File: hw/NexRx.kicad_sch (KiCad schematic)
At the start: 12 parts, among them J101 SMA

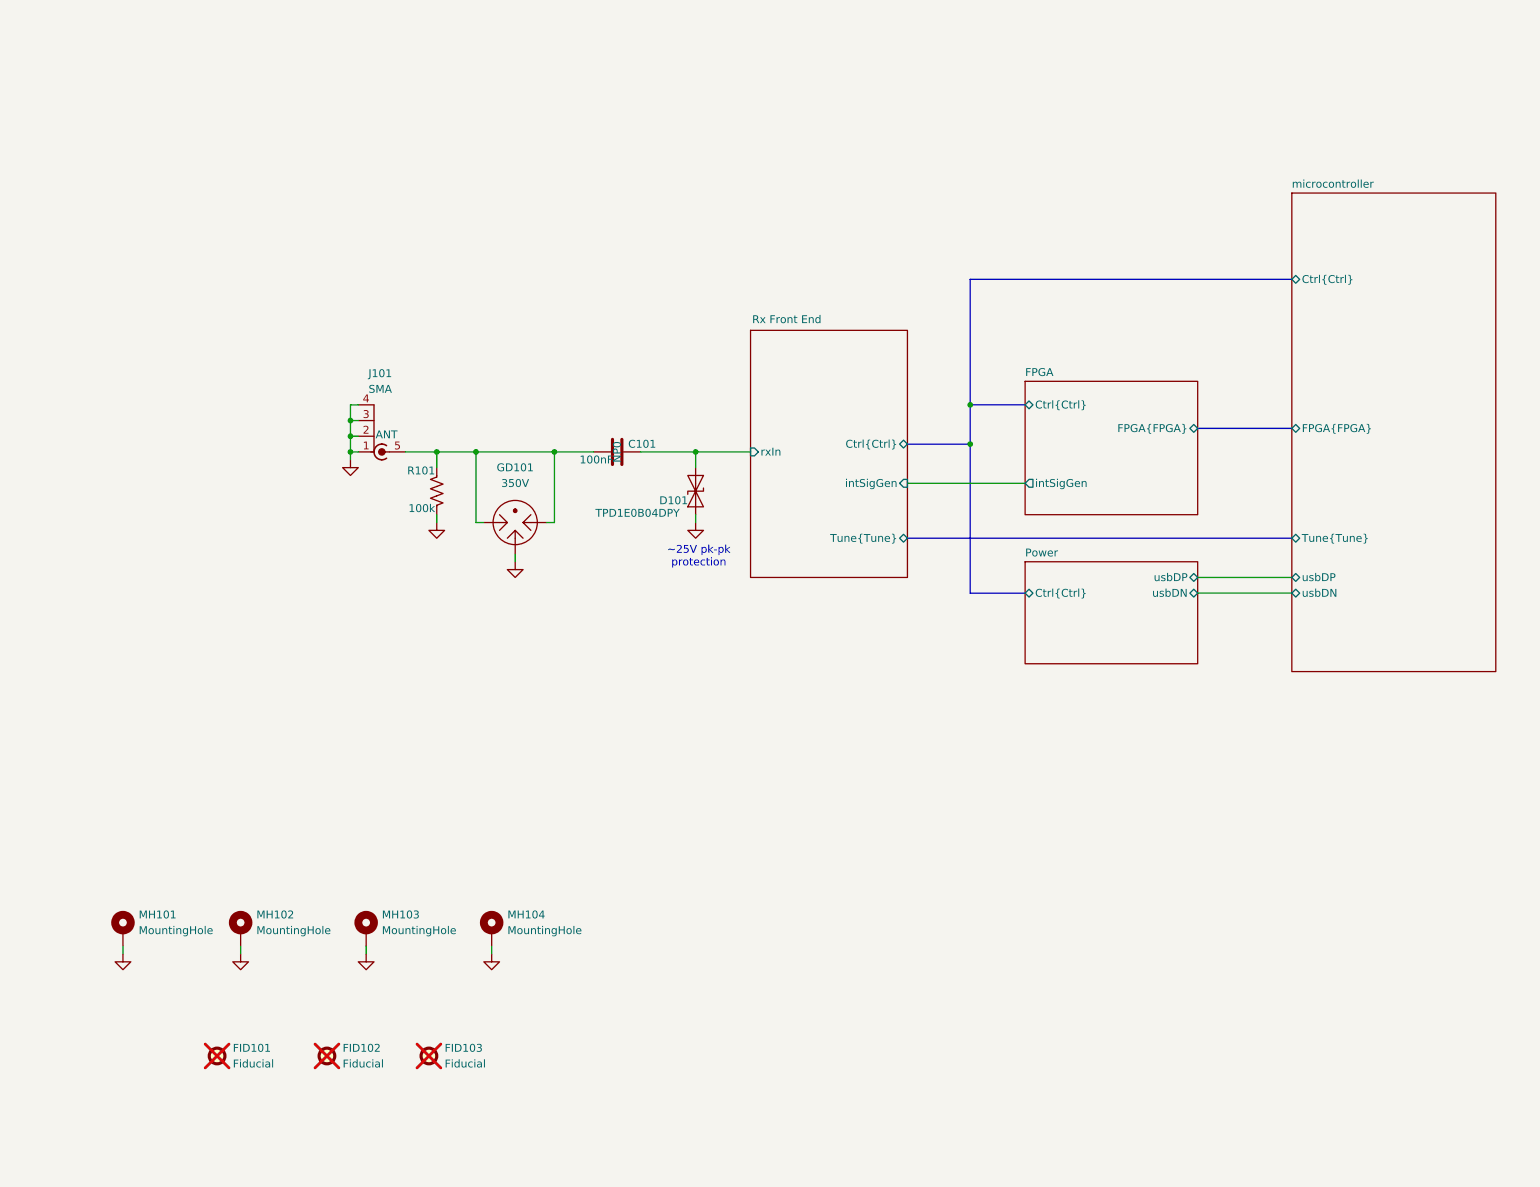
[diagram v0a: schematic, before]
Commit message: Switch from three QSDs to two Octature Sync Detectors (OSDs) and use one 4-channel TI ADC for each. Simplify. Refactor busses to use cleaner notation and modularity. Switch to a CPLD from FPGA. Eliminate STM32C011 GPIO expanders (maybe need them back later?). Power sequencing is now trivial and there is no 5VA so no boost to more than 5V then LDO back down to 5V. Merge some pages into one. Change to 74CBTLV3125 for OSD switches (four for each OSD). Elminate MAX9939 PGA since ADC has this feature. Filter the fuck outta the inputs to the ADCs.
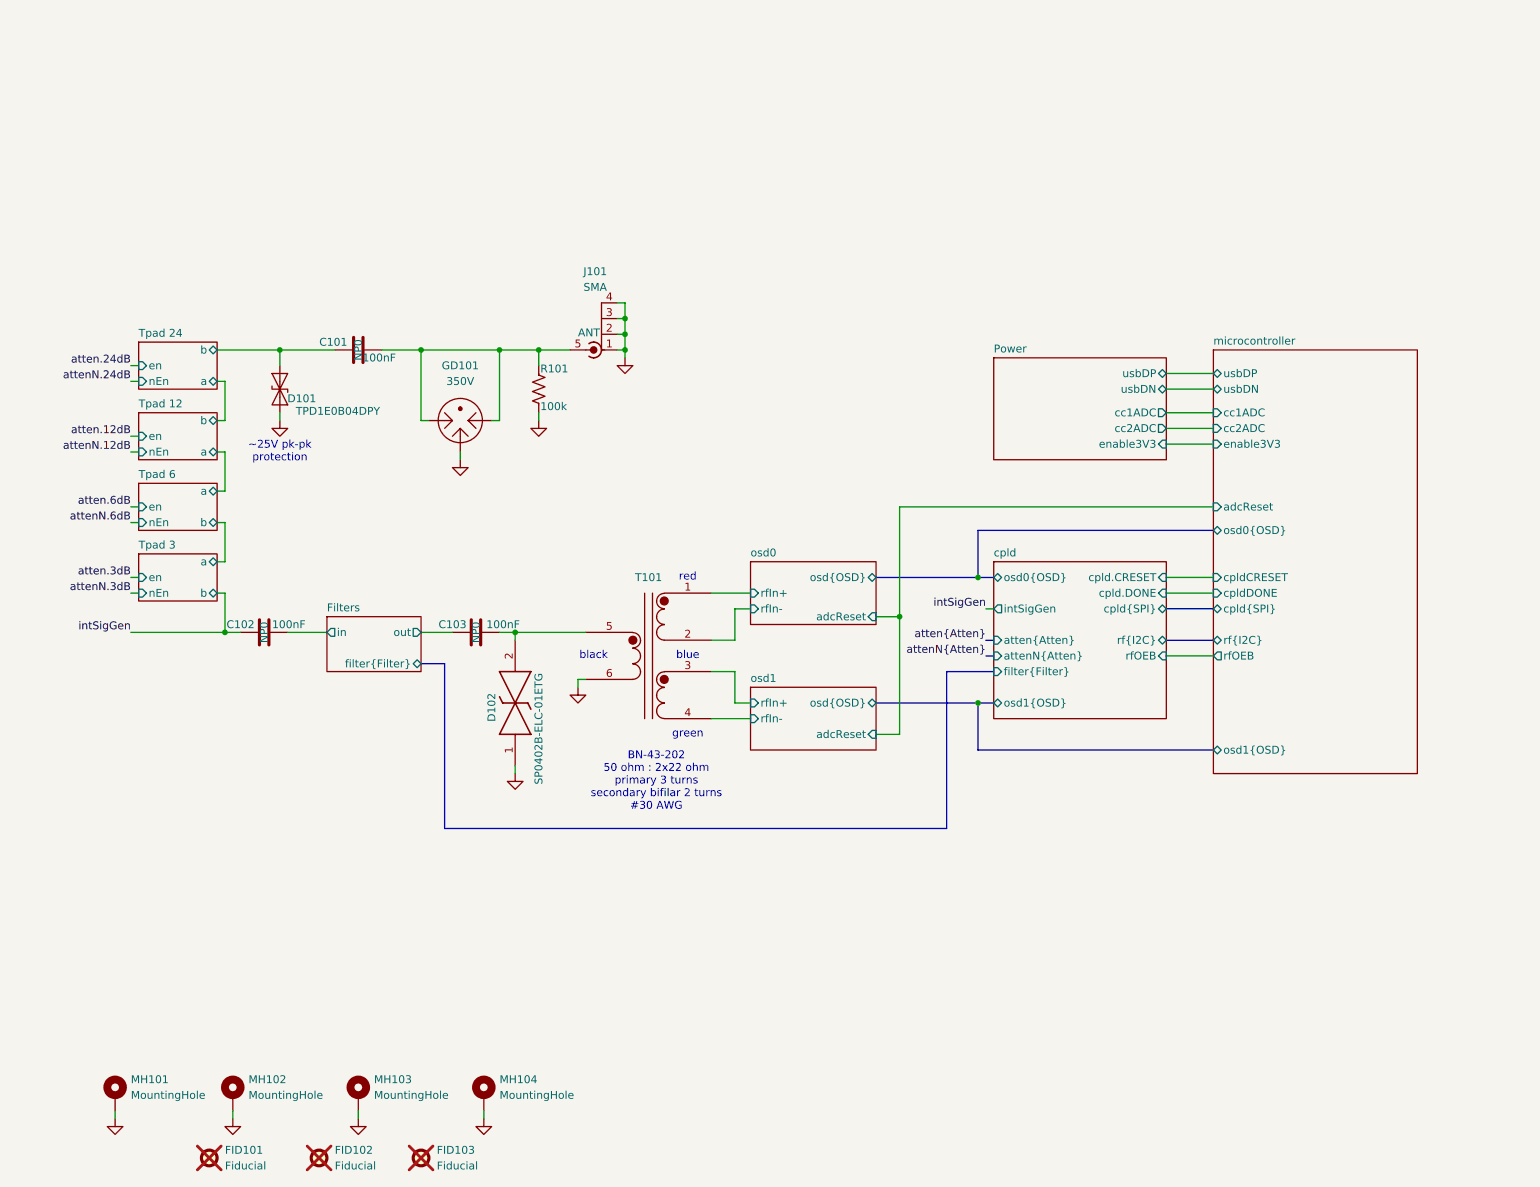
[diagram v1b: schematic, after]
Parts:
- added C102, C103: 100nF, Capacitor_SMD:C_1206_3216Metric, symbol Device:C
- added D102: SP0402B-ELC-01ETG, Diode_SMD:D_0402_1005Metric, symbol Library:SP0402B-ELC-01ETG
- added T101: BN-43-202, 50:2x22 ohm, 3 turns primary, 2 turns 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, Library:Transformer-2P-2S-BN-43-202, symbol Library:Transformer-1P-2S
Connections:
- net GND: now also D102.1, T101.6 (P1B)
- net Rx Front End/rxIn renamed Tpad 24/b
- new net: C103.2, D102.2, T101.5 (P1A)
- new net Filters/in: C102.1
- new net Filters/out: C103.1
- new net intSigGen: C102.2
- new net osd0/rfIn+: T101.1 (S1A)
- new net osd0/rfIn-: T101.2 (S1B)
- new net osd1/rfIn+: T101.3 (S2A)
- new net osd1/rfIn-: T101.4 (S2B)
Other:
- sheet FPGA renamed cpld
- removed sheet Rx Front End
- added sheet Filters (filters.kicad_sch)
- added sheet Tpad 12 (tpad.kicad_sch)
- added sheet Tpad 24 (tpad.kicad_sch)
- added sheet Tpad 3 (tpad.kicad_sch)
- added sheet Tpad 6 (tpad.kicad_sch)
- added sheet osd0 (osd.kicad_sch)
- added sheet osd1 (osd.kicad_sch)
- sheet Power ports: added cc1ADC, cc2ADC, enable3V3; removed Ctrl{Ctrl}
- sheet cpld: file fpga.kicad_sch -> cpld.kicad_sch
- sheet cpld ports: added attenN{Atten}, atten{Atten}, cpld.CRESET, cpld.DONE, cpld{SPI}, filter{Filter}, osd0{OSD}, osd1{OSD}, rfOEB, rf{I2C}; removed Ctrl{Ctrl}, FPGA{FPGA}
- sheet microcontroller ports: added adcReset, cc1ADC, cc2ADC, cpldCRESET, cpldDONE, cpld{SPI}, enable3V3, osd0{OSD}, osd1{OSD}, rfOEB, rf{I2C}; removed Ctrl{Ctrl}, FPGA{FPGA}, Tune{Tune}
- note added: "BN-43-202 50 ohm : 2x22 ohm primary 3 turns secondary bifilar 2 turns #30 AWG"
- note added: "black"
- note added: "blue"
- note added: "green"
- note added: "red"
- moved on the sheet: C101, D101, FID101, FID102, FID103, GD101, J101, MH101, MH102, MH103, MH104, R101

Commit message: Now two CPLDs, new placement for better routing of clocks and symmetry for delay. Not routed yet but placement is "complete".
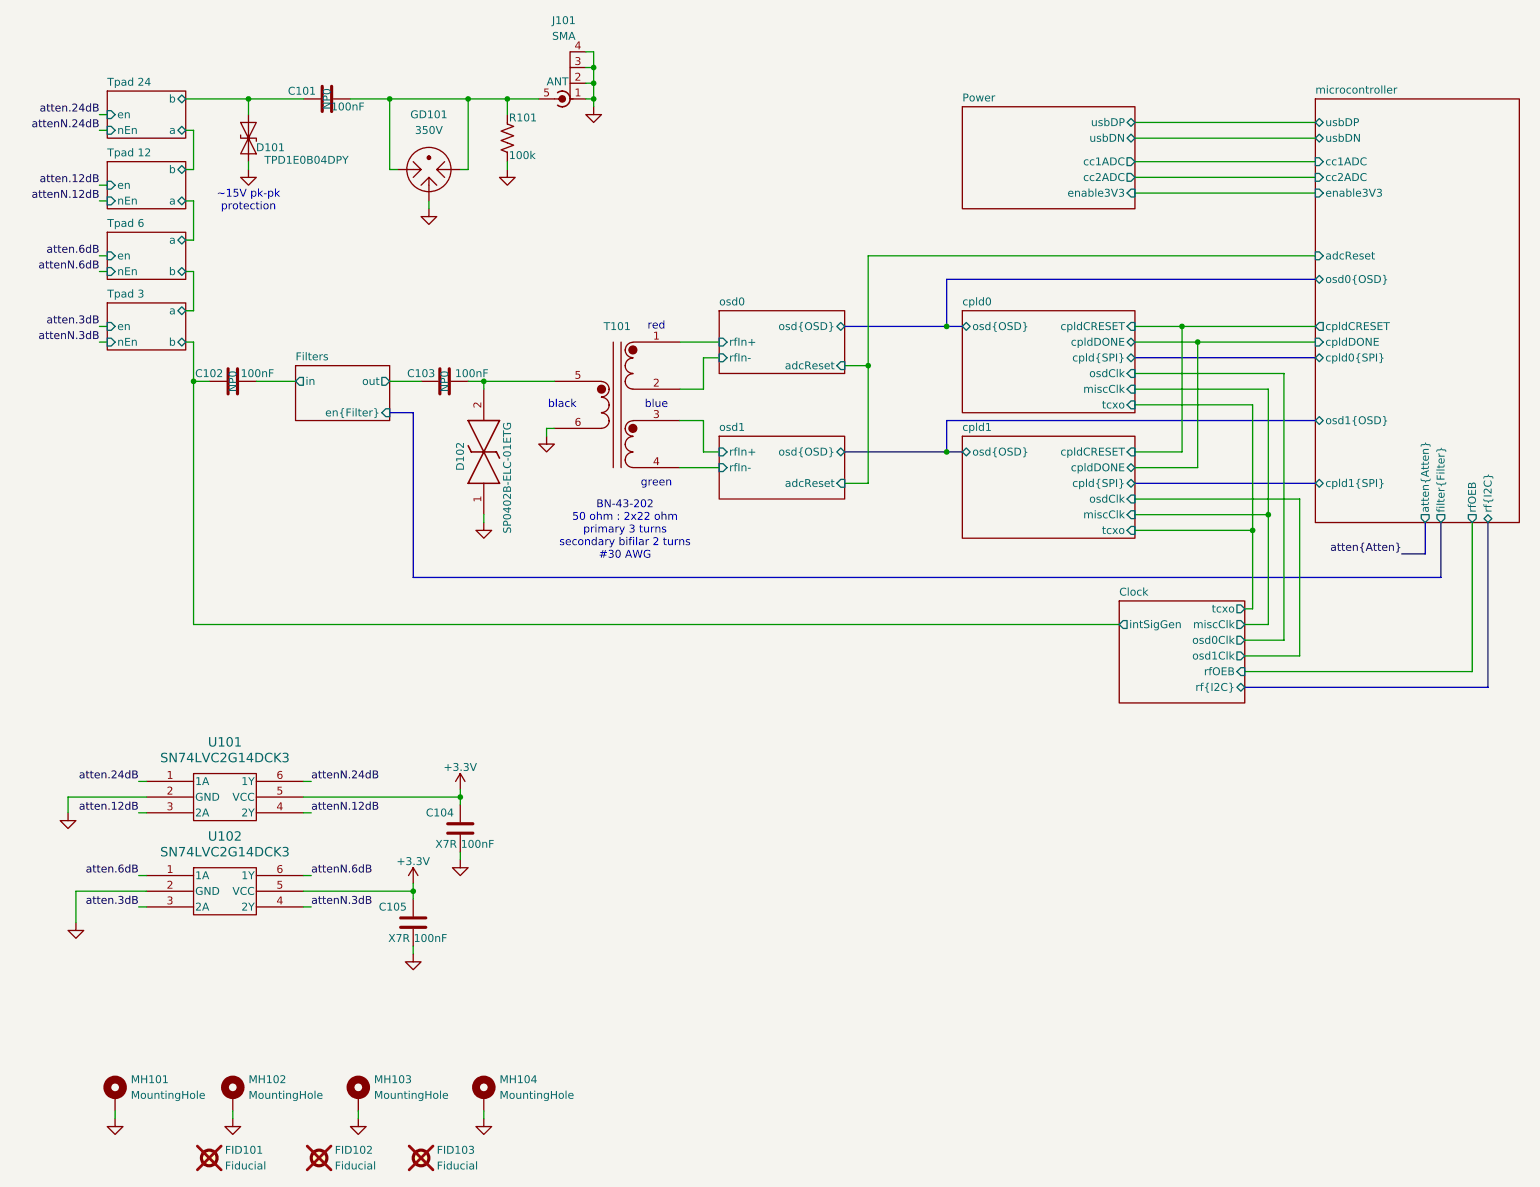
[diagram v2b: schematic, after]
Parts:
- added C104, C105: 100nF, Capacitor_SMD:C_0402_1005Metric, symbol Device:C
- added U101, U102: SN74LVC2G14DCK3, Library:SOIC_G14DCK3_TEX, symbol Library:SN74LVC2G14DCK3
- R101: footprint Resistor_SMD:R_0603_1608Metric -> Resistor_SMD:R_0402_1005Metric
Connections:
- net GND: now also C104.2, C105.2, U101.2 (GND), U102.2 (GND)
- net atten.12dB: now also U101.3 (2A)
- net atten.24dB: now also U101.1 (1A)
- net atten.3dB: now also U102.3 (2A)
- net atten.6dB: now also U102.1 (1A)
- net attenN.12dB: now also U101.4 (2Y)
- net attenN.24dB: now also U101.6 (1Y)
- net attenN.3dB: now also U102.4 (2Y)
- net attenN.6dB: now also U102.6 (1Y)
- net intSigGen renamed Clock/intSigGen
- new net +3.3V: C104.1, C105.1, U101.5 (VCC), U102.5 (VCC)
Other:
- sheet cpld renamed cpld0
- added sheet Clock (clock.kicad_sch)
- added sheet cpld1 (cpld.kicad_sch)
- sheet Filters ports: added en{Filter}; removed filter{Filter}
- sheet cpld0 ports: added cpldCRESET, cpldDONE, miscClk, osdClk, osd{OSD}, tcxo; removed attenN{Atten}, atten{Atten}, cpld.CRESET, cpld.DONE, filter{Filter}, intSigGen, osd0{OSD}, osd1{OSD}, rfOEB, rf{I2C}
- sheet microcontroller ports: added atten{Atten}, cpld0{SPI}, cpld1{SPI}, filter{Filter}; removed cpld{SPI}
- note added: "~15V pk-pk protection"
- note removed: "~25V pk-pk protection"
- moved on the sheet: C101, C102, C103, D101, D102, GD101, J101, R101, T101

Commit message: PCB and schematic both pass DRC and all nets routed. Now for some desk checking...
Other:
- sheet Clock ports: added none; removed miscClk
- sheet cpld0 ports: added none; removed miscClk
- sheet cpld1 ports: added none; removed miscClk
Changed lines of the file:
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@@
 	)
 	(junction
-		(at 219.71 93.98)
-		(diameter 0)
-		(color 0 0 0 0)
-	)
-	(junction
 		(at 88.9 139.7)
 		(diameter 0)
@@
 	(wire
 		(pts
-			(xy 219.71 111.76) (xy 215.9 111.76)
-		)
-		(stroke
-			(width 0)
-			(type default)
-		)
-	)
-	(wire
-		(pts
 			(xy 30.48 31.75) (xy 31.75 31.75)
 		)
@@
 	(wire
 		(pts
-			(xy 219.71 93.98) (xy 219.71 111.76)
-		)
-		(stroke
-			(width 0)
-			(type default)
-		)
-	)
-	(wire
-		(pts
 			(xy 44.45 38.1) (xy 45.72 38.1)
 		)
@@
 	(wire
 		(pts
-			(xy 219.71 73.66) (xy 219.71 93.98)
-		)
-		(stroke
-			(width 0)
-			(type default)
-		)
-	)
-	(wire
-		(pts
 			(xy 63.5 152.4) (xy 64.77 152.4)
 		)
@@
 	(wire
 		(pts
-			(xy 198.12 73.66) (xy 219.71 73.66)
-		)
-		(stroke
-			(width 0)
-			(type default)
-		)
-	)
-	(wire
-		(pts
 			(xy 63.5 154.94) (xy 81.28 154.94)
 		)
@@
 	(wire
 		(pts
-			(xy 219.71 93.98) (xy 198.12 93.98)
-		)
-		(stroke
-			(width 0)
-			(type default)
-		)
-	)
-	(wire
-		(pts
 			(xy 44.45 31.75) (xy 45.72 31.75)
 		)
@@
 			)
 		)
-		(pin "miscClk" input
-			(at 198.12 73.66 0)
-			(effects
-				(font
-					(size 1.27 1.27)
-				)
-				(justify right)
-			)
-		)
 		(pin "osdClk" input
 			(at 198.12 71.12 0)
@@
 			)
 		)
-		(pin "miscClk" output
-			(at 215.9 111.76 0)
-			(effects
-				(font
-					(size 1.27 1.27)
-				)
-				(justify right)
-			)
-		)
 		(pin "osd0Clk" output
 			(at 215.9 114.3 0)
@@
 			(effects
 				(font
-					(size 1.27 1.27)
-				)
-				(justify right)
-			)
-		)
-		(pin "miscClk" input
-			(at 198.12 93.98 0)
-			(effects
-				(font

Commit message: 3D rendering now. All DRCs pass on schematic and PCB. BOM scrubbed to coallesce parts. Still no part numbers for most.
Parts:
- added BT101: CR3032 holder, Library:S8401-46, symbol Library:S8401-46
- added C104, C105: 10uF, Capacitor_SMD:C_0402_1005Metric, symbol Device:C
- added C106: 150pF, Capacitor_SMD:C_0402_1005Metric, symbol Device:C
- added J102: SMA, Library:733910083, symbol Library:SMA
- added L101: 47nH, Inductor_SMD:L_0603_1608Metric, symbol Device:L_Ferrite_Small
- added U102: GNSS module, RF_GPS:ublox_MAX, symbol Library:ATGM336H-5N31
- renumbered C104 to C107, C105 to C108, U102 to U103
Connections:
- net +3.3V: now also C105.1, U102.8 (VCC)
- net GND: now also BT101.1 (-VE), C104.1, C105.2, J102.1 (In), J102.2 (Ext), J102.3 (Ext), J102.4 (Ext), U102.1 (GND), U102.10 (GND), U102.12 (GND)
- new net: C106.1, U102.11 (RF_IN)
- new net: C106.2, J102.5 (Ext), L101.2
- new net: BT101.2, BT101.3, C104.2, U102.6 (V_BCKP)
- new net: L101.1, U102.14 (VCC_RF)
- new net gnssPPS: U102.4 (PPS)
- new net microcontroller/gnssNRESET: U102.9 (~{RESET})
- new net microcontroller/gnssRx: U102.3 (RXD)
- new net microcontroller/gnssTx: U102.2 (TXD)
- no-connect marks 0 -> 3
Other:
- sheet cpld0 ports: added gnssPPS; removed none
- sheet cpld1 ports: added gnssPPS; removed none
- sheet microcontroller ports: added gnssNRESET, gnssRx, gnssTx; removed none

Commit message: Not proud of the rats nest of controls for attenuator and filter, but now I have four filters (not five), all DRC pass, 3D renders properly, and I may tidy it up a bit later.
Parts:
- C104, C105: cap-type X7R -> X5R; working-voltage 25V -> 10V
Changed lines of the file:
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@@
 			)
 		)
-		(property "working-voltage" "25V"
+		(property "working-voltage" "10V"
 			(at 168.91 123.19 90)
 			(effects
@@
 			)
 		)
-		(property "cap-type" "X7R"
+		(property "cap-type" "X5R"
 			(at 168.91 123.19 90)
 			(effects
@@
 			)
 		)
-		(property "working-voltage" "25V"
+		(property "working-voltage" "10V"
 			(at 181.61 133.35 0)
 			(effects
@@
 			)
 		)
-		(property "cap-type" "X7R"
+		(property "cap-type" "X5R"
 			(at 181.61 133.35 0)
 			(effects
